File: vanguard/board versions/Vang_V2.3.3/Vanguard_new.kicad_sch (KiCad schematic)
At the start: 103 parts, among them J1 USB_C_Receptacle_USB2.0_16P, J2 Micro_SD_Card_Det1, J3 Conn_02x03_Odd_Even, J4 Conn_01x03, J5 Conn_01x03, J6 Conn_01x03, J7 Conn_01x02_Pin, Q1 BSS138, Q2 BSS138, Q3 BSS138, Q4 BSS138, U1 TXB0104D, U11 TPS82130SILR, U12 AP2112K-3.3, U3 ATSAMD11D14A-M, U4 BMP390L, U5 BD1020HFV-TR, U6 AT25DF641A-SH-T, U7 ATmega4809-A, U8 BNO055, U9 TPS61092, Y1 Crystal

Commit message: 2.3.3 fix
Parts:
- added TP9: TestPoint, TestPoint:TestPoint_Pad_1.0x1.0mm, symbol Connector:TestPoint
- C10, C11, C16, C17, C19, C20, C21, C22, C23, C6, C7, C9: footprint (none) -> Capacitor_SMD:C_0201_0603Metric
- C3: value 0u1 -> 0.1uF
- C4: value 22p -> 22pF
- R27, R28, R29, R30, R31, R35, R37, R38: footprint (none) -> Resistor_SMD:R_0402_1005Metric
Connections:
- net GND: now also U8.17 (COM3), U8.18 (COM2), U8.5 (PS1), U8.6 (PS0)
- net SCL: now also U8.19 (COM1); no longer U8.17 (COM3)
- net SDA: now also U8.20 (COM0), TP9.1; no longer U8.18 (COM2)
- no-connect marks 38 -> 33
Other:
- moved on the sheet: C17, C19, C20, C21, C3, C4, C5, JP1, JP2, R1, R10, R2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

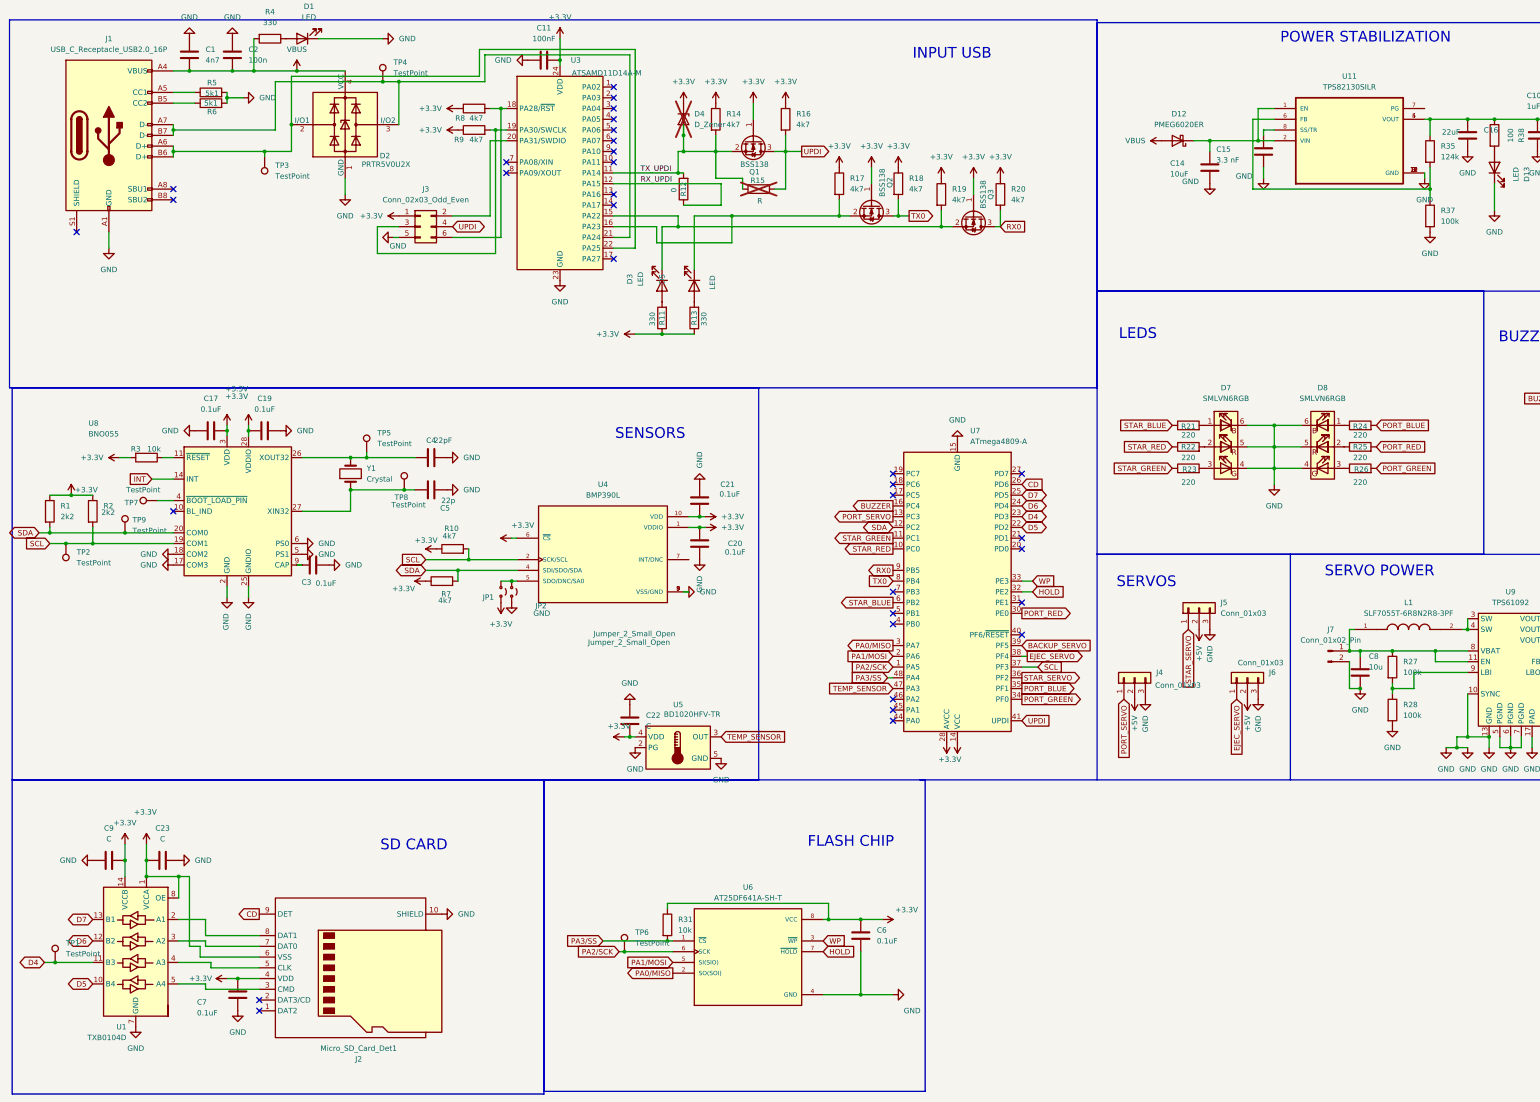
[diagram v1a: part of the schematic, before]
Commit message: made fixes check description
Removed TXB0104D(image)
removed the level shifting mosfets
U11 - changed r35 from 124k to 350, should get the output voltage up
added shield gnd

I also reassigned pins on the main mcu
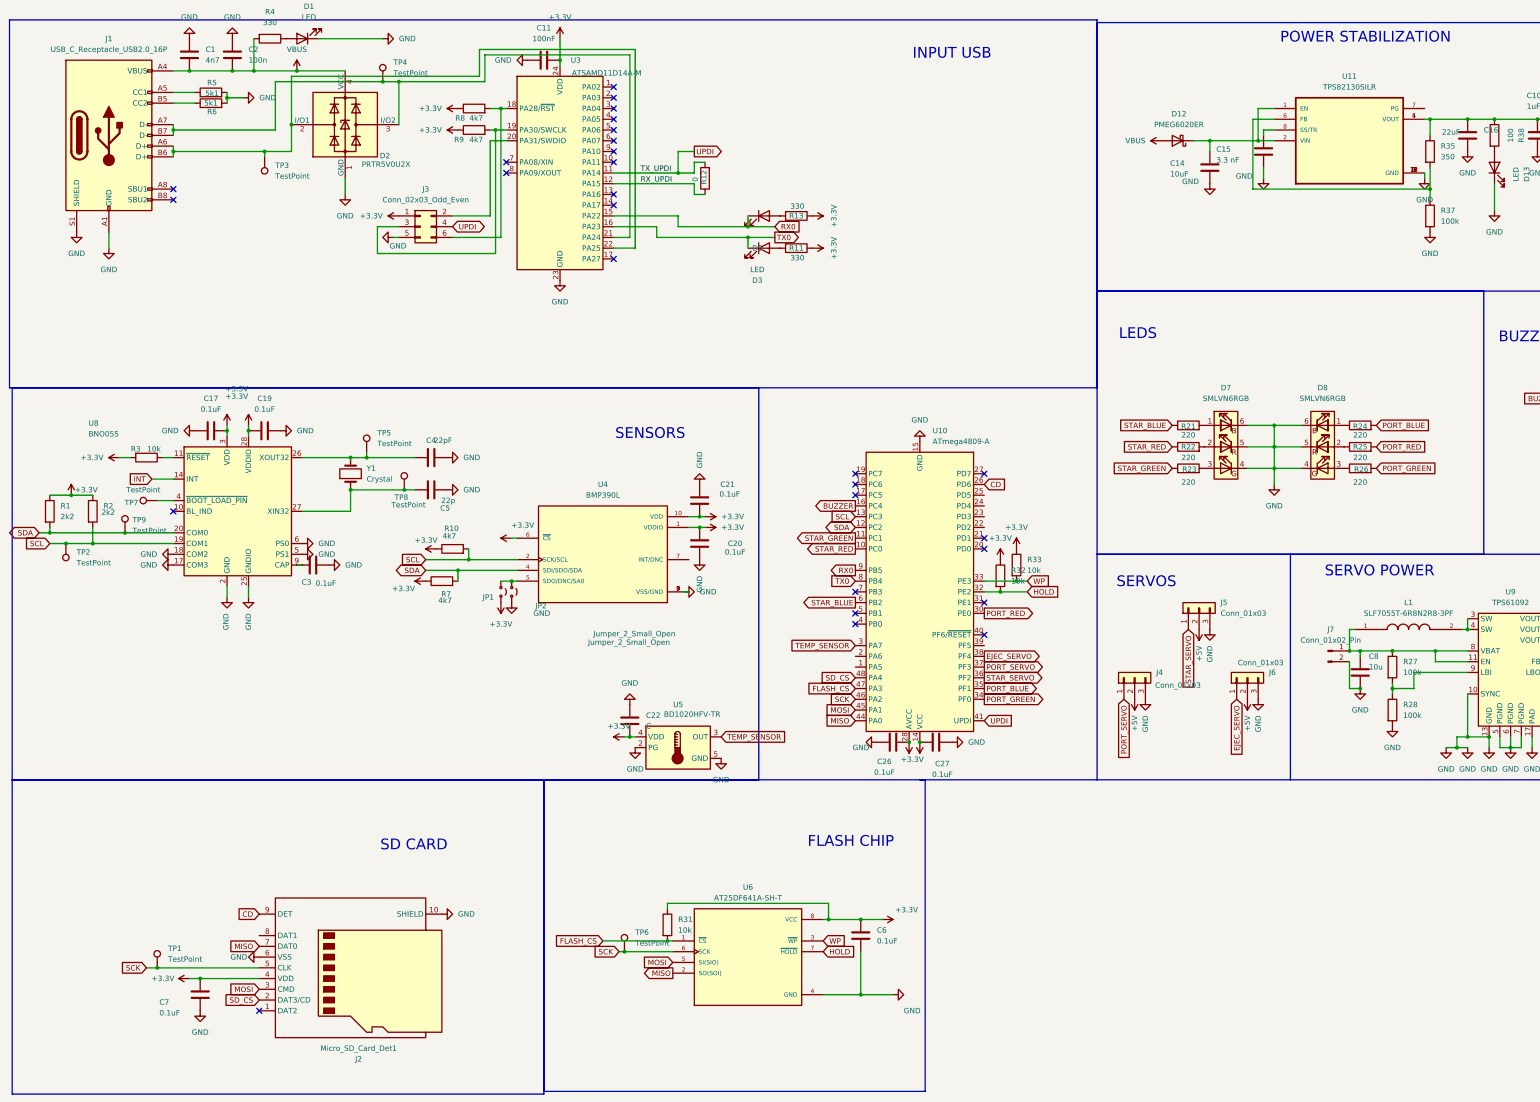
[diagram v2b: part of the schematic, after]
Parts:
- removed C23, C9: C, Capacitor_SMD:C_0201_0603Metric, symbol Device:C
- removed D4: D_Zener, symbol Device:D_Zener
- removed Q1, Q2, Q3: BSS138, Package_TO_SOT_SMD:SOT-23, symbol Transistor_FET:BSS138
- removed R14, R16, R17, R18, R19, R20: 4k7, Resistor_SMD:R_0402_1005Metric, symbol Device:R
- removed R15: R, Resistor_SMD:R_0402_1005Metric, symbol Device:R
- removed U1: TXB0104D, Package_SO:SOIC-14_3.9x8.7mm_P1.27mm, symbol Logic_LevelTranslator:TXB0104D
- removed U7: ATmega4809-A, Package_QFP:TQFP-48_7x7mm_P0.5mm, symbol MCU_Microchip_ATmega:ATmega4809-A
- added C26, C27: 0.1uF, symbol Device:C
- added R32, R33: 10k, symbol Device:R
- added U10: ATmega4809-A, Package_QFP:TQFP-48_7x7mm_P0.5mm, symbol MCU_Microchip_ATmega:ATmega4809-A
- R35: value 124k -> 350
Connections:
- net D4 is gone; now on net SCK: TP1.1
- net PA0/MISO is gone; now on net MISO: U6.2 (SO(SOI))
- net PA1/MOSI is gone; now on net MOSI: U6.5 (SI(SIO))
- net PA2/SCK is gone; now on net SCK: TP6.1, U6.6 (SCK)
- net TX_UPDI is gone; now on net UPDI: R12.2, U3.11 (PA14)
- net +3.3V: now also C26.2, C27.1, R32.1, R33.1, U10.14 (VCC), U10.28 (AVCC), U10.42 (VCC); no longer J2.6 (VSS)
- net BUZZER: now also U10.16 (PC4)
- net CD: now also U10.26 (PD6)
- net EJEC_SERVO: now also U10.38 (PF4)
- net GND: now also J1.S1 (SHIELD), J2.6 (VSS), C26.1, C27.2, U10.15 (GND), U10.29 (GND), U10.43 (GND)
- net HOLD: now also R32.2, U10.32 (PE2)
- net PORT_BLUE: now also U10.35 (PF1)
- net PORT_GREEN: now also U10.34 (PF0)
- net PORT_RED: now also U10.30 (PE0)
- net PORT_SERVO: now also U10.37 (PF3)
- net RX0: now also D5.1 (K), U3.15 (PA22), U10.9 (PB5)
- net SCL: now also U10.13 (PC3)
- net SDA: now also U10.12 (PC2)
- net STAR_BLUE: now also U10.6 (PB2)
- net STAR_GREEN: now also U10.11 (PC1)
- net STAR_RED: now also U10.10 (PC0)
- net STAR_SERVO: now also U10.36 (PF2)
- net TEMP_SENSOR: now also U10.3 (PA7)
- net TX0: now also D3.1 (K), U3.16 (PA23), U10.8 (PB4)
- net UPDI: now also U10.41 (UPDI)
- net WP: now also R33.2, U10.33 (PE3)
- net MISO: now reaches J2.7 (DAT0)
- net MISO: now also U10.44 (PA0)
- net SCK: now reaches J2.5 (CLK)
- net SCK: now also U10.46 (PA2)
- net MOSI: now reaches J2.3 (CMD)
- net MOSI: now also U10.45 (PA1)
- net SD_CS: now reaches J2.2 (DAT3/CD)
- net SD_CS: now also U10.48 (PA4)
- net PA3/SS renamed FLASH_CS
- net FLASH_CS: now also U10.47 (PA3)
- no-connect marks 33 -> 28
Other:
- moved on the sheet: C7, D3, D5, R11, R12, R13, TP1
